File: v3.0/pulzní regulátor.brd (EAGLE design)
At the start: 27.9 x 51.7 mm, 19 parts, among them Q1 NX3008, Q2 NX3008, Q3 NX3008, Q4 NX3008

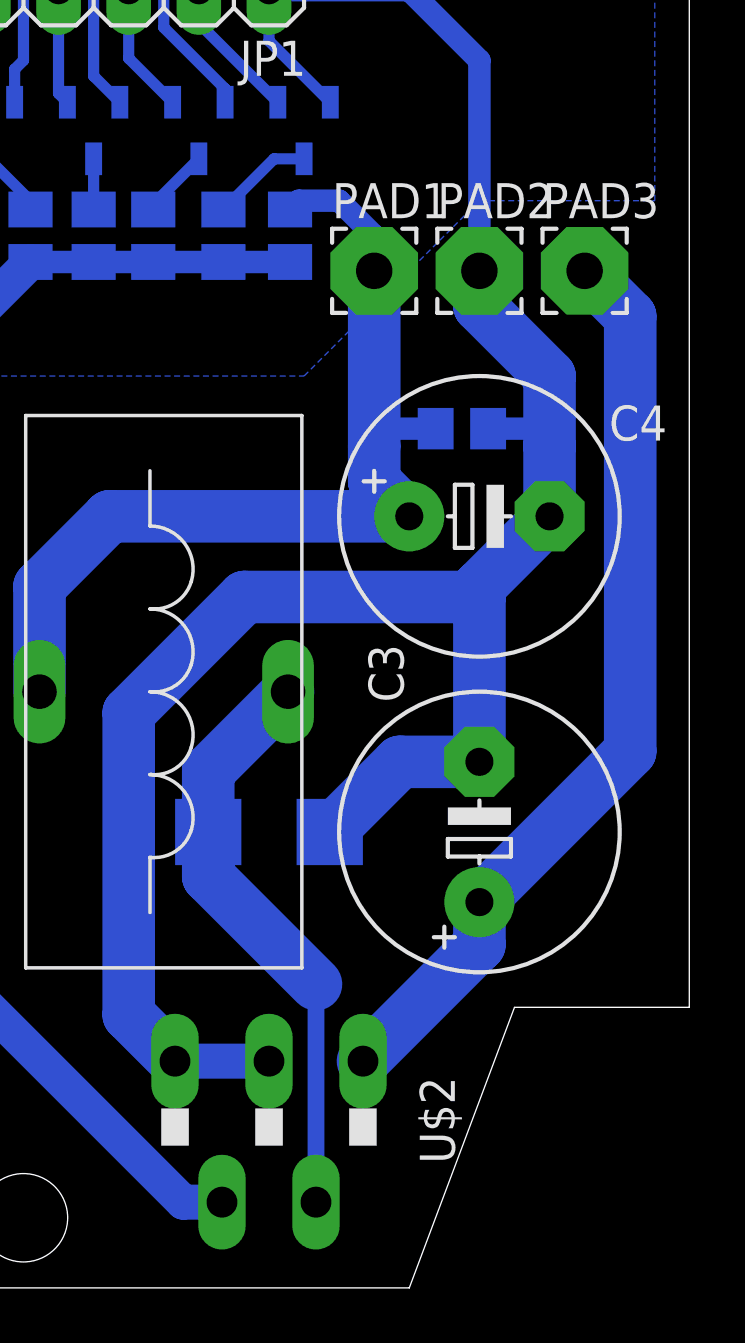
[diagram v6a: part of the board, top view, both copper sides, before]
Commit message: zpřehledněno schéma spínaného zdroje a dokončena jeho dokumentace
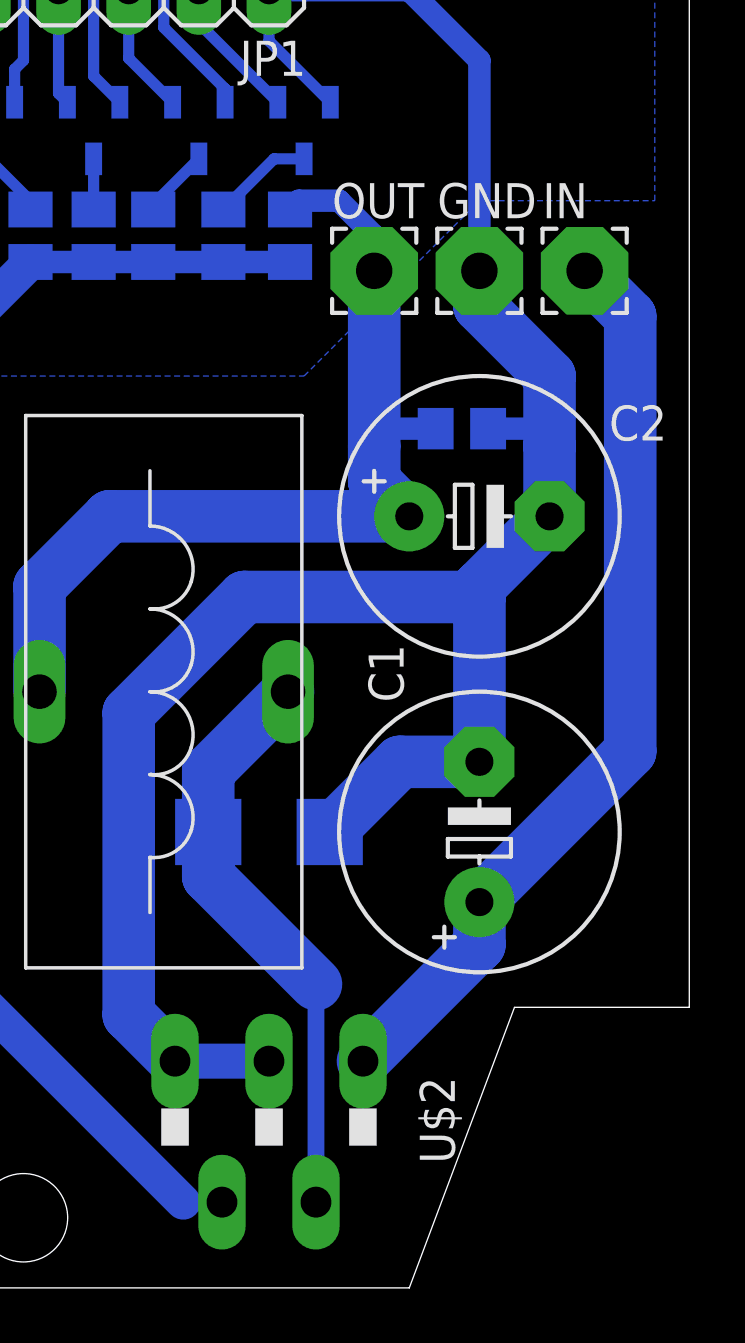
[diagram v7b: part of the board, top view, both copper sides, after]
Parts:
- C1, C2: value (none) -> 1000uF/35V
- D2: value MBRS130LT3 -> B340A
- L1: value DTMSSDTMSS-16/0,033/6,0 -> 47uH/3A
- Q1, Q2, Q3, Q4: value NX3008 -> 2N7002
- R1: value 1K5 -> 15K
- R2: value 4K3 -> 1K5
- R3: value 5K1 -> 3K3
- R4: value 6K8 -> 5K1
- R5: value 15K -> 6K8
- R6: value (none) -> 100K
- moved R1 9.40 mm to (13.5, 39.4), turned to 90 degrees
- moved R4 2.54 mm to (8.51, 39.4)
- moved R5 2.41 mm to (11.0, 39.4), turned to 270 degrees
- moved R2 2.29 mm to (4.06, 39.4)
- moved R3 2.16 mm to (6.35, 39.4)
- renumbered C3 to C1, C4 to C2, PAD1 to OUT, PAD2 to GND, PAD3 to IN, U$4 to L1
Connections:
- removed net N$6: R1.2, R2.2, R3.2, R4.2, R5.1, U$2.4
- new net FEEDBACK: R1.1, R2.2, R3.2, R4.2, R5.2, U$2.4
- net N$1: now also R5.1; no longer R4.1
- net N$11: now also R3.1; no longer R2.1
- net N$12: now also R4.1; no longer R3.1
- net N$7: now also R2.1; no longer R1.1
- net VCC: now also R1.2; no longer R5.2
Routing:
- net N$6: track 49.1 -> 0.00 mm
- net FEEDBACK: track 0.00 -> 47.7 mm

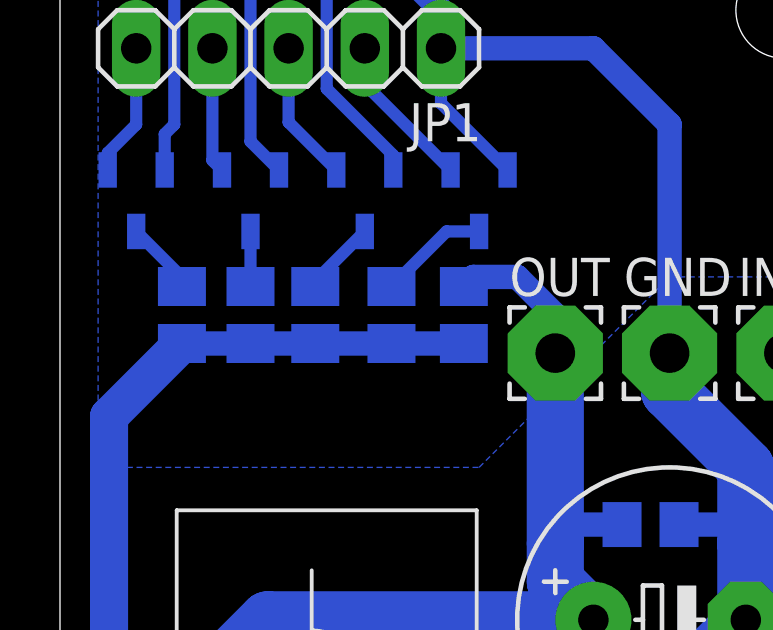
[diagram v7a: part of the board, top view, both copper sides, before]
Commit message: přidání 3D modelu úpravy dokumentace
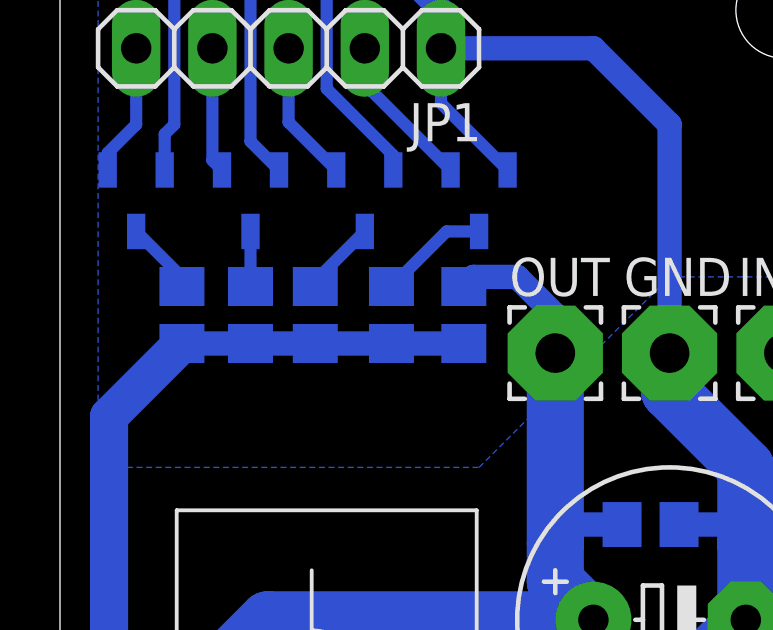
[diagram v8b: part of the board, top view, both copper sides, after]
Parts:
- R1, R2, R3, R4, R5: device rcl_my:M0805 -> rcl:R0805
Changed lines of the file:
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@@
 </layers>
 <board>
-<fusionsync huburn="a.YnVzaW5lc3M6c3BzdHJ1dG5vdjM" projecturn="a.YnVzaW5lc3M6c3BzdHJ1dG5vdjMjMjAyMDAzMzEyODExMTAyMDY" f3durn="urn:adsk.wipprod:dm.lineage:Wyhkb4j1T3y43OJJPs_q7g" pcbguid="c6696d83-4a0f-42e7-b2fc-2a2a6b268699" lastpulledtime="" lastsyncedchangeguid="5f48968b-f0e6-1f98-428d-cf6b1e6b6569"/>
+<fusionsync huburn="a.YnVzaW5lc3M6c3BzdHJ1dG5vdjM" projecturn="a.YnVzaW5lc3M6c3BzdHJ1dG5vdjMjMjAyMDAzMzEyODExMTAyMDY" f3durn="urn:adsk.wipprod:dm.lineage:Wyhkb4j1T3y43OJJPs_q7g" pcbguid="c6696d83-4a0f-42e7-b2fc-2a2a6b268699" lastpulledtime="" lastsyncedchangeguid="2df68b37-39ab-9caf-65c0-231cbd5ef188"/>
 <plain>
 <wire x1="0" y1="1.27" x2="17.78" y2="1.27" width="0" layer="20"/>
@@
 <attribute name="VALUE" x="13.97" y="51.435" size="1.27" layer="27" rot="R180"/>
 </element>
-<element name="OUT" library="wirepad" library_urn="urn:adsk.eagle:library:412" package="3,17/1,3" package3d_urn="urn:adsk.eagle:package:30833/1" value="" x="16.51" y="38.1" smashed="yes">
+<element name="OUT" library="wirepad" library_urn="urn:adsk.eagle:library:412" package="3,17/1,3" package3d_urn="urn:adsk.eagle:package:30833/1" override_package3d_urn="urn:adsk.eagle:package:33936895/2" override_package_urn="urn:adsk.eagle:footprint:30815/1" value="" x="16.51" y="38.1" smashed="yes">
 <attribute name="NAME" x="14.986" y="40.005" size="1.27" layer="25" ratio="10"/>
 <attribute name="POPULARITY" value="3" x="58.42" y="10.16" size="1.778" layer="27" display="off"/>
 <attribute name="VALUE" x="16.51" y="39.3" size="0.0254" layer="27"/>
 </element>
-<element name="GND" library="wirepad" library_urn="urn:adsk.eagle:library:412" package="3,17/1,3" package3d_urn="urn:adsk.eagle:package:30833/1" value="" x="20.32" y="38.1" smashed="yes">
+<element name="GND" library="wirepad" library_urn="urn:adsk.eagle:library:412" package="3,17/1,3" package3d_urn="urn:adsk.eagle:package:30833/1" override_package3d_urn="urn:adsk.eagle:package:33936879/2" override_package_urn="urn:adsk.eagle:footprint:30815/1" value="" x="20.32" y="38.1" smashed="yes">
 <attribute name="NAME" x="18.796" y="40.005" size="1.27" layer="25" ratio="10"/>
 <attribute name="POPULARITY" value="3" x="68.58" y="10.16" size="1.778" layer="27" display="off"/>
 <attribute name="VALUE" x="20.32" y="39.3" size="0.0254" layer="27"/>
 </element>
-<element name="IN" library="wirepad" library_urn="urn:adsk.eagle:library:412" package="3,17/1,3" package3d_urn="urn:adsk.eagle:package:30833/1" value="" x="24.13" y="38.1" smashed="yes">
+<element name="IN" library="wirepad" library_urn="urn:adsk.eagle:library:412" package="3,17/1,3" package3d_urn="urn:adsk.eagle:package:30833/1" override_package3d_urn="urn:adsk.eagle:package:33936877/2" override_package_urn="urn:adsk.eagle:footprint:30815/1" value="" x="24.13" y="38.1" smashed="yes">
 <attribute name="NAME" x="22.606" y="40.005" size="1.27" layer="25" ratio="10"/>
 <attribute name="POPULARITY" value="3" x="40.64" y="3.81" size="1.778" layer="27" display="off"/>
 <attribute name="VALUE" x="24.13" y="39.3" size="0.0254" layer="27"/>
 </element>
-<element name="Q1" library="NEXPERIA " package="SOT95P240X110-3N" value="2N7002" x="2.54" y="43.18" smashed="yes" rot="MR270">
+<element name="Q1" library="NEXPERIA " package="SOT95P240X110-3N" override_package3d_urn="urn:adsk.eagle:package:33936901/2" override_package_urn="urn:adsk.eagle:footprint:33936902/1" value="2N7002" x="2.54" y="43.18" smashed="yes" rot="MR270">
 <attribute name="NAME" x="2.54" y="40.005" size="1.27" layer="26" ratio="10" rot="MR270"/>
 <attribute name="VALUE" x="4.445" y="40.005" size="1.27" layer="28" ratio="10" rot="MR270"/>
 </element>
-<element name="Q2" library="NEXPERIA " package="SOT95P240X110-3N" value="2N7002" x="6.35" y="43.18" smashed="yes" rot="MR270">
+<element name="Q2" library="NEXPERIA " package="SOT95P240X110-3N" override_package3d_urn="urn:adsk.eagle:package:33936871/2" override_package_urn="urn:adsk.eagle:footprint:33936872/1" value="2N7002" x="6.35" y="43.18" smashed="yes" rot="MR270">
 <attribute name="NAME" x="6.35" y="40.005" size="1.27" layer="26" ratio="10" rot="MR270"/>
 <attribute name="VALUE" x="8.255" y="40.005" size="1.27" layer="28" ratio="10" rot="MR270"/>
 </element>
-<element name="Q3" library="NEXPERIA " package="SOT95P240X110-3N" value="2N7002" x="10.16" y="43.18" smashed="yes" rot="MR270">
+<element name="Q3" library="NEXPERIA " package="SOT95P240X110-3N" override_package3d_urn="urn:adsk.eagle:package:33936865/2" override_package_urn="urn:adsk.eagle:footprint:33936866/1" value="2N7002" x="10.16" y="43.18" smashed="yes" rot="MR270">
 <attribute name="NAME" x="10.16" y="40.005" size="1.27" layer="26" ratio="10" rot="MR270"/>
 <attribute name="VALUE" x="12.065" y="40.005" size="1.27" layer="28" ratio="10" rot="MR270"/>
 </element>
-<element name="Q4" library="NEXPERIA " package="SOT95P240X110-3N" value="2N7002" x="13.97" y="43.18" smashed="yes" rot="MR270">
+<element name="Q4" library="NEXPERIA " package="SOT95P240X110-3N" override_package3d_urn="urn:adsk.eagle:package:33936903/2" override_package_urn="urn:adsk.eagle:footprint:33936905/1" value="2N7002" x="13.97" y="43.18" smashed="yes" rot="MR270">
 <attribute name="NAME" x="13.97" y="40.005" size="1.27" layer="26" ratio="10" rot="MR270"/>
 <attribute name="VALUE" x="15.875" y="40.005" size="1.27" layer="28" ratio="10" rot="MR270"/>
 </element>
-<element name="R2" library="rcl_my" package="M0805" value="1K5" x="4.064" y="39.37" smashed="yes" rot="MR270">
+<element name="R2" library="rcl" library_urn="urn:adsk.eagle:library:334" package="R0805" package3d_urn="urn:adsk.eagle:package:23553/2" value="1K5" x="4.064" y="39.37" smashed="yes" rot="MR270">
 <attribute name="NAME" x="2.794" y="40.64" size="1.27" layer="26" rot="MR270"/>
+<attribute name="POPULARITY" value="86" x="4.064" y="39.37" size="1.778" layer="28" rot="MR270" display="off"/>
+<attribute name="SPICEPREFIX" value="R" x="4.064" y="39.37" size="1.778" layer="28" rot="MR270" display="off"/>
 <attribute name="VALUE" x="6.604" y="40.64" size="1.27" layer="28" rot="MR270"/>
 </element>
-<element name="R3" library="rcl_my" package="M0805" value="3K3" x="6.35" y="39.37" smashed="yes" rot="MR270">
+<element name="R3" library="rcl" library_urn="urn:adsk.eagle:library:334" package="R0805" package3d_urn="urn:adsk.eagle:package:23553/2" value="3K3" x="6.35" y="39.37" smashed="yes" rot="MR270">
 <attribute name="NAME" x="5.08" y="40.64" size="1.27" layer="26" rot="MR270"/>
+<attribute name="POPULARITY" value="86" x="6.35" y="39.37" size="1.778" layer="28" rot="MR270" display="off"/>
+<attribute name="SPICEPREFIX" value="R" x="6.35" y="39.37" size="1.778" layer="28" rot="MR270" display="off"/>
 <attribute name="VALUE" x="8.89" y="40.64" size="1.27" layer="28" rot="MR270"/>
 </element>
-<element name="R4" library="rcl_my" package="M0805" value="5K1" x="8.509" y="39.37" smashed="yes" rot="MR270">
+<element name="R4" library="rcl" library_urn="urn:adsk.eagle:library:334" package="R0805" package3d_urn="urn:adsk.eagle:package:23553/2" value="5K1" x="8.509" y="39.37" smashed="yes" rot="MR270">
 <attribute name="NAME" x="7.239" y="40.64" size="1.27" layer="26" rot="MR270"/>
+<attribute name="POPULARITY" value="86" x="8.509" y="39.37" size="1.778" layer="28" rot="MR270" display="off"/>
+<attribute name="SPICEPREFIX" value="R" x="8.509" y="39.37" size="1.778" layer="28" rot="MR270" display="off"/>
 <attribute name="VALUE" x="11.049" y="40.64" size="1.27" layer="28" rot="MR270"/>
 </element>
-<element name="R5" library="rcl_my" package="M0805" value="6K8" x="11.049" y="39.37" smashed="yes" rot="MR270">
+<element name="R5" library="rcl" library_urn="urn:adsk.eagle:library:334" package="R0805" package3d_urn="urn:adsk.eagle:package:23553/2" value="6K8" x="11.049" y="39.37" smashed="yes" rot="MR270">
 <attribute name="NAME" x="9.779" y="40.64" size="1.27" layer="26" rot="MR270"/>
+<attribute name="POPULARITY" value="86" x="11.049" y="39.37" size="1.778" layer="28" rot="MR270" display="off"/>
+<attribute name="SPICEPREFIX" value="R" x="11.049" y="39.37" size="1.778" layer="28" rot="MR270" display="off"/>
 <attribute name="VALUE" x="13.589" y="40.64" size="1.27" layer="28" rot="MR270"/>
 </element>
-<element name="R1" library="rcl_my" package="M0805" value="15K" x="13.462" y="39.37" smashed="yes" rot="MR90">
+<element name="R1" library="rcl" library_urn="urn:adsk.eagle:library:334" package="R0805" package3d_urn="urn:adsk.eagle:package:23553/2" value="15K" x="13.462" y="39.37" smashed="yes" rot="MR90">
 <attribute name="NAME" x="14.732" y="38.1" size="1.27" layer="26" rot="MR90"/>
+<attribute name="POPULARITY" value="86" x="13.462" y="39.37" size="1.778" layer="28" rot="MR90" display="off"/>
+<attribute name="SPICEPREFIX" value="R" x="13.462" y="39.37" size="1.778" layer="28" rot="MR90" display="off"/>
 <attribute name="VALUE" x="10.922" y="38.1" size="1.27" layer="28" rot="MR90"/>
 </element>
-<element name="U$2" library="regulators" package="TO220-5" value="AP1501TO220" x="12.7" y="1.27" smashed="yes" rot="R180">
+<element name="U$2" library="regulators" package="TO220-5" override_package3d_urn="urn:adsk.eagle:package:33936918/2" override_package_urn="urn:adsk.eagle:footprint:4814/1" value="AP1501TO220" x="12.7" y="1.27" smashed="yes" rot="R180">
 <attribute name="NAME" x="18.161" y="8.9154" size="1.27" layer="25" ratio="10" rot="R270"/>
 <attribute name="VALUE" x="5.969" y="8.9154" size="1.27" layer="27" ratio="10" rot="R270"/>
@@
 packages will not be understood (or retained) with this version.
 </note>
+<note version="9.4" severity="warning">
+Since Version 9.4, EAGLE supports the overriding of 3D packages
+in schematics and board files. Those overridden 3d packages
+will not be understood (or retained) with this version.
+</note>
 </compatibility>
